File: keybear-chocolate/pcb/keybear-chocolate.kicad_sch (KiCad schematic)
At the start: 99 parts, among them J1 MJ-4PP-9, J2 BATT, J3 LED, J4 OLED, SW1 SW_PUSH, SW10 SW_PUSH, SW11 SW_PUSH, SW12 SW_PUSH, SW13 SW_PUSH, SW14 SW_PUSH, SW15 SW_PUSH, SW16 SW_PUSH, SW17 SW_PUSH, SW18 SW_PUSH, SW19 SW_PUSH, SW2 SW_PUSH, SW20 SW_PUSH, SW21 SW_PUSH, SW22 SW_PUSH, SW25 Rotary_Encoder_Switch, SW3 SW_PUSH, SW30 BATT_SW, SW4 SW_PUSH, SW5 SW_PUSH, SW6 SW_PUSH, SW7 SW_PUSH, SW8 SW_PUSH, SW9 SW_PUSH, U1 ProMicro

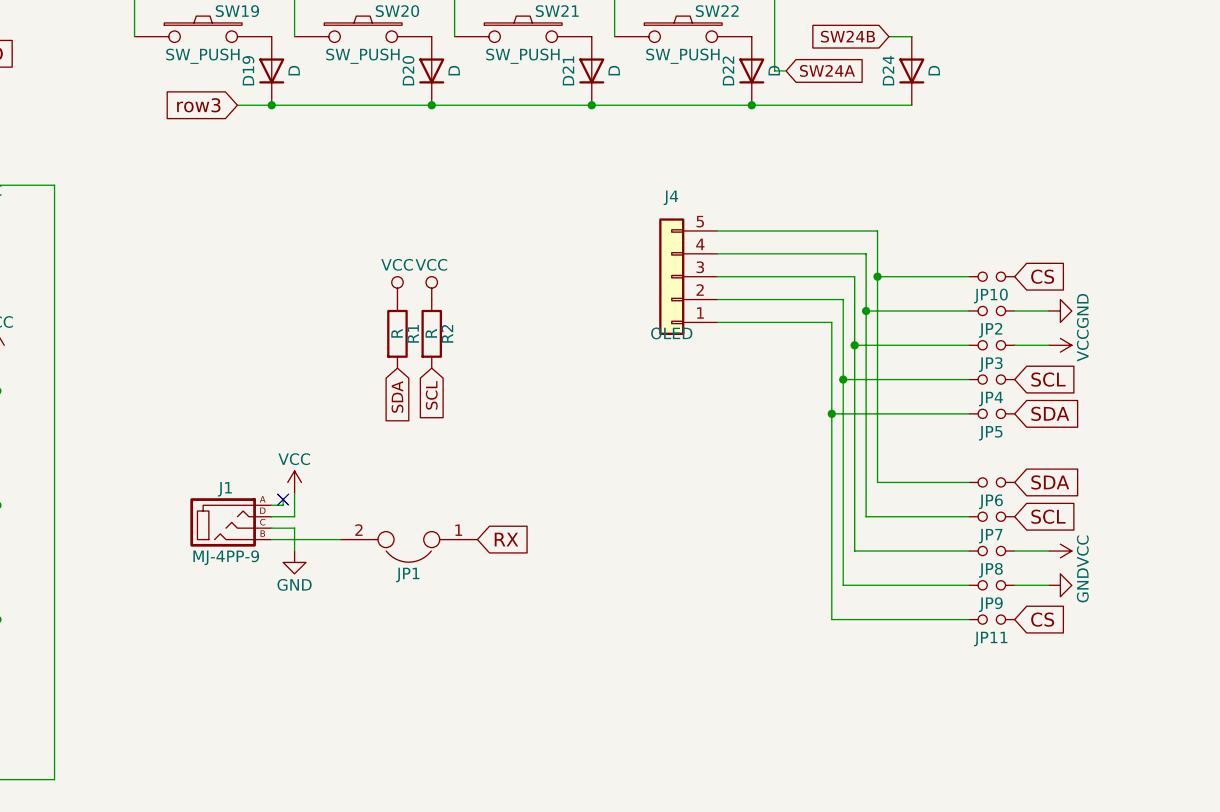
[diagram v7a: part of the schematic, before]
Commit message: board will be able to do uart or i2c communication between boards
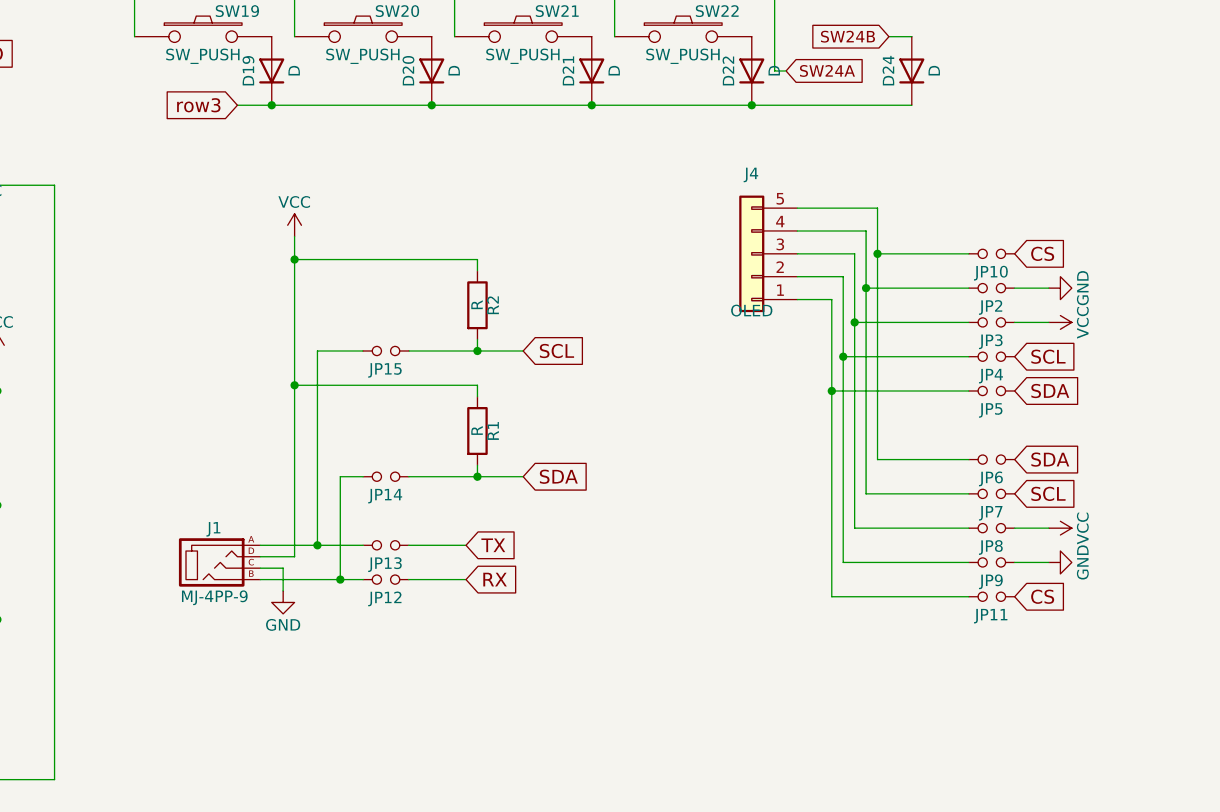
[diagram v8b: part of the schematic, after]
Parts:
- removed JP1: (no value), kbd:JPC2, symbol corne-chocolate-rescue:Jumper-Device
- added JP12, JP13, JP14, JP15: (no value), kbd:Jumper, symbol corne-chocolate-rescue:Jumper_NO_Small-Device
- R1, R2: footprint SofleKeyboard-footprint:RESISTOR_mini -> Resistor_SMD:R_1206_3216Metric
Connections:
- net RX: now also JP12.1
- net SCL: now also JP15.1
- net SDA: now also JP14.1
- net TX: now also JP13.1
- net at J1.B: now also JP12.2, JP14.2
- net at J1.A: now also JP13.2, JP15.2
- no-connect marks 3 -> 2
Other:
- moved on the sheet: J1, J4, JP10, JP11, JP2, JP3, JP4, JP5, JP6, JP7, JP8, JP9
